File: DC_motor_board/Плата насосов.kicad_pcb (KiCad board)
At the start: 2 copper layers, 77.5 x 64.5 mm, 106 parts, among them J1 Prog, J2 OUT DG142R-5.08-02P-14, J3 OUT DG142R-5.08-02P-14, J4 IN24V DG142R-5.08-04P-14, U1 ADM3485EARZ-REEL, U2 ISO6741FDWR, U3 STM32G070RBTx, U4 AM1SS-2403SJZ, U5 BTS7960b, U6 BTS7960b, U7 BTS7960b, U8 BTS7960b, U9 ULN2003D1013TR

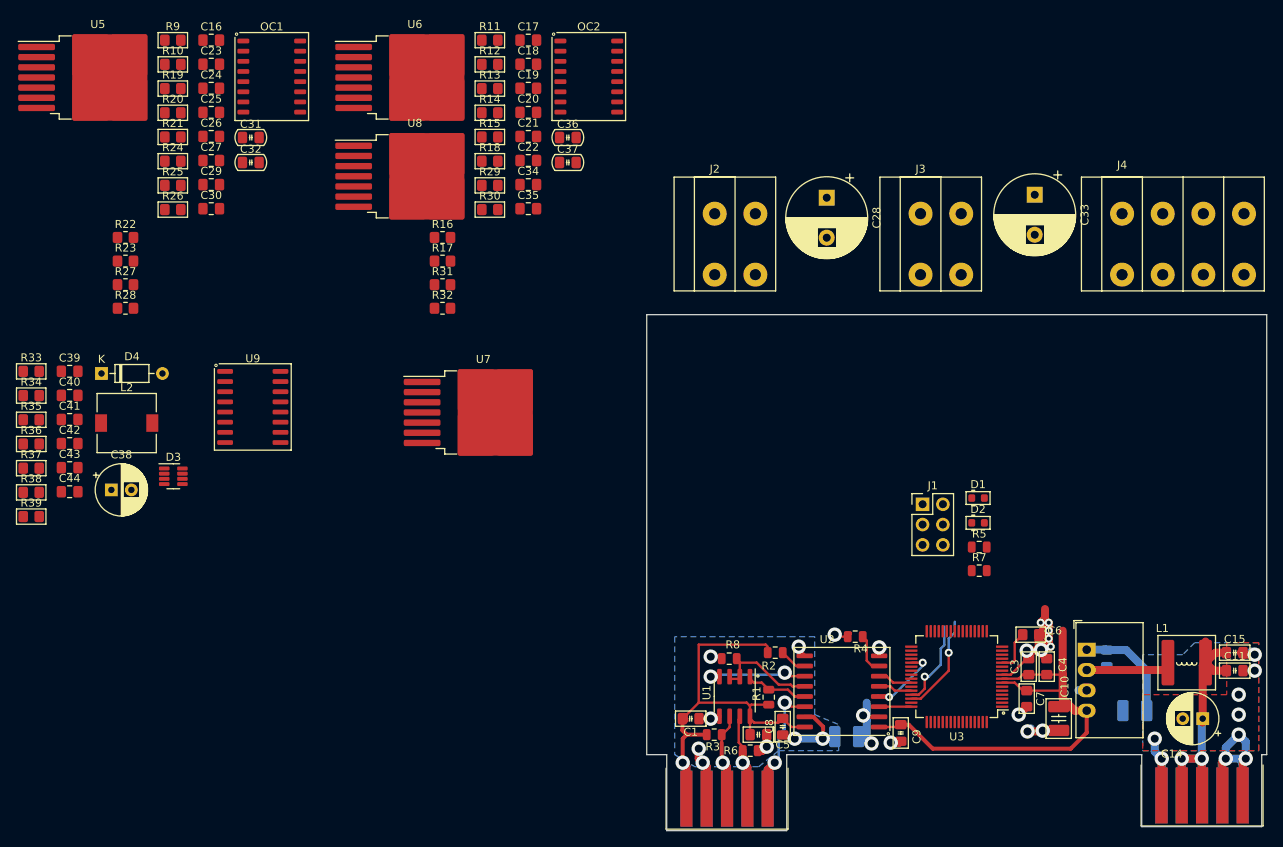
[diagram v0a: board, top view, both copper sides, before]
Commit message: Renew footprint connectors PCB
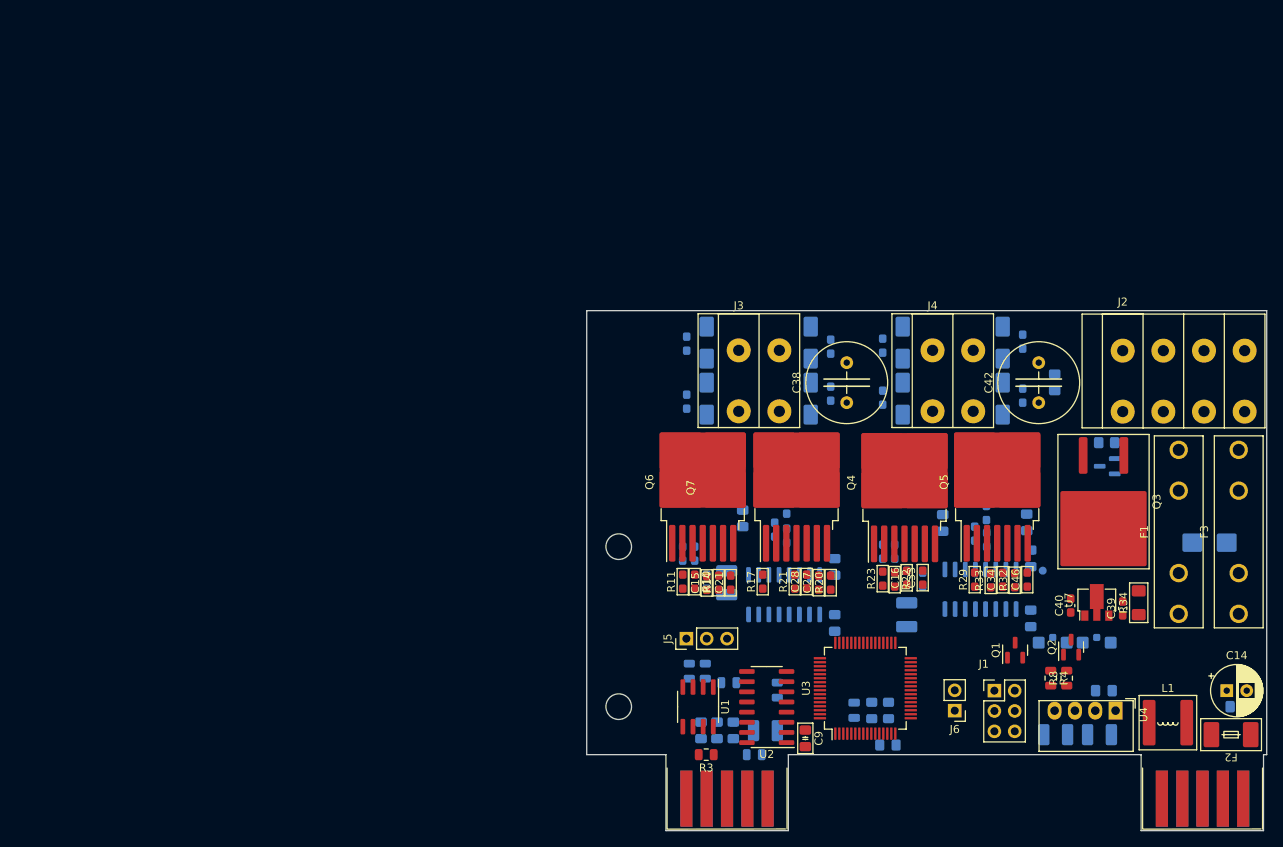
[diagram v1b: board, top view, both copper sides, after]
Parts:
- removed C43: 0,1uF 50V 0805, Capacitor_SMD:C_0805_2012Metric_Pad1.18x1.45mm_HandSolder
- removed C44: 33pF 50V 0805, Capacitor_SMD:C_0805_2012Metric_Pad1.18x1.45mm_HandSolder
- removed L2: 4,7uH 3A (MDH7045C-4R7NB=P3), Inductor_SMD:L_7.3x7.3_H4.5
- removed OC1, OC2: IS281- 4, PCM_Package_SO_AKL:SOIC-16W_5.3x10.2mm_P1.27mm
- removed R35: 104 0805, PCM_Resistor_SMD_AKL:R_0805_2012Metric_Pad1.20x1.40mm_HandSolder
- removed R36: 203 0805, PCM_Resistor_SMD_AKL:R_0805_2012Metric_Pad1.20x1.40mm_HandSolder
- removed R37: 413 0805, PCM_Resistor_SMD_AKL:R_0805_2012Metric_Pad1.20x1.40mm_HandSolder
- removed R38: 752 0805, PCM_Resistor_SMD_AKL:R_0805_2012Metric_Pad1.20x1.40mm_HandSolder
- removed R39: 912 0805, PCM_Resistor_SMD_AKL:R_0805_2012Metric_Pad1.20x1.40mm_HandSolder
- removed U8: BTS7960b, Package_TO_SOT_SMD:TO-263-7_TabPin8
- removed U9: ULN2003D1013TR, PCM_Package_SO_AKL:SO-16_5.3x10.2mm_P1.27mm
- added C45: 270 pf X7R 1206 2000v 202R18W271KW4E, PCM_Capacitor_SMD_Handsoldering_AKL:C_1210_3225Metric_Pad1.42x2.65mm, B.Cu at (129.0, 103.5)
- added C46: 1nF 50V 0603, PCM_Resistor_SMD_AKL:R_0603_1608Metric_Pad1.05x0.95mm_HandSolder, F.Cu at (144.1, 99.1)
- added D10: STPS2H100A, Diode_SMD:D_SMA, B.Cu at (141.0, 76.5)
- added D11: STPS2H100A, Diode_SMD:D_SMA, B.Cu at (117.0, 69.5)
- added D12: STPS2H100A, Diode_SMD:D_SMA, B.Cu at (141.0, 69.5)
- added D5: STPS2H100A, Diode_SMD:D_SMA, B.Cu at (104.0, 69.5)
- added D6: STPS2H100A, Diode_SMD:D_SMA, B.Cu at (128.5, 69.5)
- added D7: STPS2H100A, Diode_SMD:D_SMA, B.Cu at (104.0, 76.5)
- added D8: STPS2H100A, Diode_SMD:D_SMA, B.Cu at (128.5, 76.5)
- added D9: STPS2H100A, Diode_SMD:D_SMA, B.Cu at (117.0, 76.5)
- added F1: Fuse 5A ZH266 (2 клипсы), Fuse:Fuseholder_100_series_5x20mm_D1,5, F.Cu at (163.0, 103.4)
- added F2: 0452.500MRL, PCM_Fuse_Handsoldering_AKL:Fuse_Littelfuse-NANO2-451_453, F.Cu at (169.5, 118.5)
- added F3: Fuse 5A ZH266 (2 клипсы), Fuse:Fuseholder_100_series_5x20mm_D1,5, F.Cu at (170.5, 103.4)
- added H1: MountingHole, MountingHole:MountingHole_3.2mm_M3, F.Cu at (93.0, 95.0)
- added H2: MountingHole, MountingHole:MountingHole_3.2mm_M3, F.Cu at (93.0, 115.0)
- added J5: DebugUSART (PinHeader_01x03_P2.54mm), Connector_PinHeader_2.54mm:PinHeader_1x03_P2.54mm_Vertical, F.Cu at (101.5, 106.5)
- added J6: Debug GPIO (PinHeader_01x02_P2.54mm), Connector_PinHeader_2.54mm:PinHeader_1x02_P2.54mm_Vertical, F.Cu at (135.0, 115.5)
- added Q1: DTC114ECA (SOT-23), Package_TO_SOT_SMD:SOT-23, F.Cu at (142.6, 107.9)
- added Q2: DTC114ECA (SOT-23), Package_TO_SOT_SMD:SOT-23, F.Cu at (149.6, 107.6)
- added Q3: IRF4905SPbF (D2PAK), PCM_Package_TO_SOT_SMD_AKL:TO-263-2, F.Cu at (153.6, 89.4)
- added Q4: BTN8962TA, Package_TO_SOT_SMD:TO-263-7_TabPin8, F.Cu at (128.7, 87.0)
- added Q5: BTN8962TA, Package_TO_SOT_SMD:TO-263-7_TabPin8, F.Cu at (140.3, 86.9)
- added Q6: BTN8962TA, Package_TO_SOT_SMD:TO-263-7_TabPin8, F.Cu at (103.5, 86.9)
- added Q7: BTN8962TA, Package_TO_SOT_SMD:TO-263-7_TabPin8, F.Cu at (115.2, 86.9)
- added TP1: TestPoint, PCM_4ms_TestPoint:TestPoint_D1, B.Cu at (146.0, 98.0)
- C1, C10, C11, C5, C8, R6: moved to B.Cu
- C13, C2: value 270 pf X7R 1206 2000v 202R18W271KW4E -> 270 pf X7R 1206 2000v 202R18W271KW4E
- C15: value 0,1uF 100V 0805 -> 0,1uF 50V 0603; footprint PCM_Capacitor_SMD_AKL:C_0805_2012Metric_Pad1.18x1.45mm_HandSolder -> PCM_Capacitor_SMD_AKL:C_0603_1608Metric_Pad1.08x0.95mm_HandSolder
- C16, C34: value 0.1uF -> 0,1uF 50V 0603; footprint Capacitor_SMD:C_0805_2012Metric_Pad1.18x1.45mm_HandSolder -> PCM_Capacitor_SMD_AKL:C_0603_1608Metric_Pad1.08x0.95mm_HandSolder
- C17, C20, C24, C25, C29: value 0.1uF -> 0,22uF 100V 0603; footprint Capacitor_SMD:C_0805_2012Metric_Pad1.18x1.45mm_HandSolder -> PCM_Resistor_SMD_AKL:R_0603_1608Metric_Pad1.05x0.95mm_HandSolder; moved to B.Cu
- C18, C19, C22, C23, C30, C35: value 0.1uF -> 0,1uF 100V 0805; footprint Capacitor_SMD:C_0805_2012Metric_Pad1.18x1.45mm_HandSolder -> PCM_Capacitor_SMD_AKL:C_0805_2012Metric_Pad1.18x1.45mm_HandSolder; moved to B.Cu
- C21, C27: value 0.1uF -> 1nF 50V 0603; footprint Capacitor_SMD:C_0805_2012Metric_Pad1.18x1.45mm_HandSolder -> PCM_Resistor_SMD_AKL:R_0603_1608Metric_Pad1.05x0.95mm_HandSolder
- C26: value 0.1uF -> 270 pf X7R 1206 2000v 202R18W271KW4E; footprint Capacitor_SMD:C_0805_2012Metric_Pad1.18x1.45mm_HandSolder -> PCM_Capacitor_SMD_Handsoldering_AKL:C_1210_3225Metric_Pad1.42x2.65mm; moved to B.Cu
- C28: value 330uF 63V -> 0,1uF 50V 0603; footprint Capacitor_THT:CP_Radial_D10.0mm_P5.00mm -> PCM_Capacitor_SMD_AKL:C_0603_1608Metric_Pad1.08x0.95mm_HandSolder
- C3: value 0,1uF 50V 0805 -> 0,1uF 100V 0805; footprint PCM_Resistor_SMD_AKL:R_0805_2012Metric_Pad1.20x1.40mm_HandSolder -> PCM_Capacitor_SMD_Handsoldering_AKL:C_0805_2012Metric_Pad1.15x1.40mm; moved to B.Cu
- C31: value 470nF 50V 0805 -> 0,1uF 100V 0805; footprint PCM_Capacitor_SMD_Handsoldering_AKL:C_0805_2012Metric_Pad1.18x1.45mm -> PCM_Capacitor_SMD_AKL:C_0805_2012Metric_Pad1.18x1.45mm_HandSolder; moved to B.Cu
- C32, C36, C37: value 470nF 50V 0805 -> 0,22uF 100V 0603; footprint PCM_Capacitor_SMD_Handsoldering_AKL:C_0805_2012Metric_Pad1.18x1.45mm -> PCM_Resistor_SMD_AKL:R_0603_1608Metric_Pad1.05x0.95mm_HandSolder; moved to B.Cu
- C33: value 330uF 63V -> 1nF 50V 0603; footprint Capacitor_THT:CP_Radial_D10.0mm_P5.00mm -> PCM_Resistor_SMD_AKL:R_0603_1608Metric_Pad1.05x0.95mm_HandSolder
- C38: value 22uF 63V (К50-35) -> 330uF 50V D10 H17; footprint Capacitor_THT:CP_Radial_D6.3mm_P2.50mm -> PCM_Capacitor_THT_AKL:C_Radial_D10.0mm_H16.0mm_P5.00mm
- C39: value 0,1uF 50V 0805 -> 0,33uF 50V 0603; footprint Capacitor_SMD:C_0805_2012Metric_Pad1.18x1.45mm_HandSolder -> Capacitor_SMD:C_0603_1608Metric_Pad1.08x0.95mm_HandSolder
- C4: footprint PCM_Resistor_SMD_AKL:R_0805_2012Metric_Pad1.20x1.40mm_HandSolder -> PCM_Capacitor_SMD_AKL:C_0805_2012Metric_Pad1.15x1.40mm; moved to B.Cu
- C40: value 22uF 16V 0805 -> 0,1uF 50V 0603; footprint Capacitor_SMD:C_0805_2012Metric_Pad1.18x1.45mm_HandSolder -> Capacitor_SMD:C_0603_1608Metric_Pad1.08x0.95mm_HandSolder
- C41: value 22uF 16V 0805 -> 0,1uF 100V 0805; footprint Capacitor_SMD:C_0805_2012Metric_Pad1.18x1.45mm_HandSolder -> PCM_Capacitor_SMD_AKL:C_0805_2012Metric_Pad1.18x1.45mm_HandSolder; moved to B.Cu
- C42: value 0,1uF 50V 0805 -> 330uF 50V D10 H17; footprint Capacitor_SMD:C_0805_2012Metric_Pad1.18x1.45mm_HandSolder -> PCM_Capacitor_THT_AKL:C_Radial_D10.0mm_H16.0mm_P5.00mm
- C6: value 0,1uF 50V 0805 -> 0,1uF 100V 0805; footprint PCM_Resistor_SMD_AKL:R_0805_2012Metric_Pad1.20x1.40mm_HandSolder -> PCM_Capacitor_SMD_AKL:C_0805_2012Metric_Pad1.15x1.40mm; moved to B.Cu
- C7: value 0,1uF 50V 0805 -> 0,1uF 100V 0805; footprint PCM_Resistor_SMD_AKL:R_0805_2012Metric_Pad1.20x1.40mm_HandSolder -> PCM_Capacitor_SMD_AKL:C_0805_2012Metric; moved to B.Cu
- D1, D2: value LED 0603 -> KPA-3010CGCK; footprint PCM_Diode_SMD_AKL:D_0603_1608Metric_TVS -> LED_SMD:LED_Kingbright_KPA-3010_3x2x1mm; moved to B.Cu
- D3: value MP2315S TSOT-23-8 -> SM6T30СA (SMB); footprint Package_TO_SOT_SMD:TSOT-23-8 -> Diode_SMD:D_SMB; moved to B.Cu
- D4: value 1N4148 SOD27 -> BZX84C10 (SOT-23); footprint Diode_THT:D_DO-35_SOD27_P7.62mm_Horizontal -> Package_TO_SOT_SMD:SOT-23; moved to B.Cu
- J2: value OUT DG142R-5.08-02P-14 -> DG142R-5.08-04P-14 IN24V; footprint Connector:DG142R-5.08-02P-14 -> Connector:DG142R-5.08-04P-14
- J3: value OUT DG142R-5.08-02P-14 -> DG142R-5.08-02P-14 OUT
- J4: value IN24V DG142R-5.08-04P-14 -> DG142R-5.08-02P-14 OUT; footprint Connector:DG142R-5.08-04P-14 -> Connector:DG142R-5.08-02P-14
- R1: value 103 0805 -> 472 0805; moved to B.Cu
- R10, R11: value 511 0805 -> 104 0603; footprint PCM_Resistor_SMD_AKL:R_0805_2012Metric_Pad1.20x1.40mm_HandSolder -> PCM_Resistor_SMD_AKL:R_0603_1608Metric_Pad1.05x0.95mm_HandSolder
- R12, R13, R19: value 511 0805 -> 103 0603; footprint PCM_Resistor_SMD_AKL:R_0805_2012Metric_Pad1.20x1.40mm_HandSolder -> PCM_Resistor_SMD_AKL:R_0603_1608Metric_Pad1.05x0.95mm_HandSolder; moved to B.Cu
- R14, R20: value 511 0805 -> 102 0603; footprint PCM_Resistor_SMD_AKL:R_0805_2012Metric_Pad1.20x1.40mm_HandSolder -> PCM_Resistor_SMD_AKL:R_0603_1608Metric_Pad1.05x0.95mm_HandSolder
- R15, R26: value 103 0805 -> 102 0603; footprint PCM_Resistor_SMD_AKL:R_0805_2012Metric_Pad1.20x1.40mm_HandSolder -> PCM_Resistor_SMD_AKL:R_0603_1608Metric_Pad1.05x0.95mm_HandSolder; moved to B.Cu
- R16, R28: value 1k -> 104 0603; footprint Resistor_SMD:R_0805_2012Metric_Pad1.20x1.40mm_HandSolder -> PCM_Resistor_SMD_AKL:R_0603_1608Metric_Pad1.05x0.95mm_HandSolder; moved to B.Cu
- R17, R22, R23: value 1k -> 104 0603; footprint Resistor_SMD:R_0805_2012Metric_Pad1.20x1.40mm_HandSolder -> PCM_Resistor_SMD_AKL:R_0603_1608Metric_Pad1.05x0.95mm_HandSolder
- R18, R24, R25, R30: value 103 0805 -> 103 0603; footprint PCM_Resistor_SMD_AKL:R_0805_2012Metric_Pad1.20x1.40mm_HandSolder -> PCM_Resistor_SMD_AKL:R_0603_1608Metric_Pad1.05x0.95mm_HandSolder; moved to B.Cu
- R2: value 472 0805 -> 103 0805; moved to B.Cu
- R21: value 103 0805 -> 102 0603; footprint PCM_Resistor_SMD_AKL:R_0805_2012Metric_Pad1.20x1.40mm_HandSolder -> PCM_Resistor_SMD_AKL:R_0603_1608Metric_Pad1.05x0.95mm_HandSolder
- R27: value 1k -> 102 0603; footprint Resistor_SMD:R_0805_2012Metric_Pad1.20x1.40mm_HandSolder -> PCM_Resistor_SMD_AKL:R_0603_1608Metric_Pad1.05x0.95mm_HandSolder; moved to B.Cu
- R29: value 103 0805 -> 104 0603; footprint PCM_Resistor_SMD_AKL:R_0805_2012Metric_Pad1.20x1.40mm_HandSolder -> PCM_Resistor_SMD_AKL:R_0603_1608Metric_Pad1.05x0.95mm_HandSolder
- R31: value 1k -> 103 0603; footprint Resistor_SMD:R_0805_2012Metric_Pad1.20x1.40mm_HandSolder -> PCM_Resistor_SMD_AKL:R_0603_1608Metric_Pad1.05x0.95mm_HandSolder; moved to B.Cu
- R32: value 1k -> 102 0603; footprint Resistor_SMD:R_0805_2012Metric_Pad1.20x1.40mm_HandSolder -> PCM_Resistor_SMD_AKL:R_0603_1608Metric_Pad1.05x0.95mm_HandSolder
- R33: value 100 0805 -> 102 0603; footprint PCM_Resistor_SMD_AKL:R_0805_2012Metric_Pad1.20x1.40mm_HandSolder -> PCM_Resistor_SMD_AKL:R_0603_1608Metric_Pad1.05x0.95mm_HandSolder
- R34: value 304 0805 -> 621 1206; footprint PCM_Resistor_SMD_AKL:R_0805_2012Metric_Pad1.20x1.40mm_HandSolder -> PCM_Resistor_SMD_AKL:R_1206_3216Metric_Pad1.42x1.75mm_HandSolder
- R4: value 472 0805 -> 151 0805
- R5: value 151 0805 -> 472 0805; moved to B.Cu
- R7: value 151 0805 -> 103 0805; moved to B.Cu
- R8: value 103 0805 -> 151 0805
- R9: value 511 0805 -> 103 0805; moved to B.Cu
- U1: value ADM3485EARZ-REEL -> ADM3485EARZ-REEL (SOIC-8)
- U2: value ISO6741FDWR -> π141M30; footprint PCM_Package_SO_AKL:SOIC-16W_7.5x10.3mm_P1.27mm -> Package_SO:SOIC-16_3.9x9.9mm_P1.27mm
- U3: value STM32G070RBTx -> STM32G070RBTx (LQFP-64)
- U4: footprint Converter_DCDC:Converter_DCDC_Murata_MEE3SxxxxSC_THT -> Converter_DCDC:Converter_DCDC_Murata_MEE1SxxxxSC_THT
- U5, U6: value BTS7960b -> π162M30; footprint Package_TO_SOT_SMD:TO-263-7_TabPin8 -> Package_SO:SOIC-16_3.9x9.9mm_P1.27mm; moved to B.Cu
- U7: value BTS7960b -> L78L05 (SOT89-3); footprint Package_TO_SOT_SMD:TO-263-7_TabPin8 -> Package_TO_SOT_SMD:SOT-89-3
- moved R34 140.8 mm to (158.0, 102.0), turned to 90 degrees
- moved C39 134.9 mm to (156.0, 102.7), turned to 90 degrees
- moved D3 129.8 mm to (166.8, 94.5)
- moved C40 127.9 mm to (149.5, 102.4), turned to 90 degrees
- moved R9 127.1 mm to (154.0, 82.0), turned to 180 degrees
- moved D4 126.3 mm to (154.1, 85.0), turned to 180 degrees
- moved C41 123.2 mm to (147.5, 74.5), turned to 90 degrees
- moved R33 122.8 mm to (139.5, 99.2), turned to 90 degrees
- moved C42 121.2 mm to (145.5, 77.0), turned to 90 degrees
- moved C30 114.5 mm to (144.5, 104.0), turned to 90 degrees
- moved C31 110.8 mm to (144.5, 96.5), turned to 90 degrees
- moved R28 110.6 mm to (139.0, 90.8), turned to 90 degrees
- moved C16 109.9 mm to (129.0, 98.9), turned to 90 degrees
- moved C23 107.9 mm to (133.5, 92.0), turned to 90 degrees
- moved U5 107.4 mm to (113.7, 101.0), turned to 90 degrees
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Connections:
- net /DE renamed /DE_USART_1
- net /DI renamed /RX_USART_1
- net /RO renamed /TX_USART_1
- C15 pad 1: +24V -> GND2
- C15 pad 2: GNDA -> Net-(Q6-SR)
- C16 pad 1: +3V3 -> GND2
- C16 pad 2: GNDD -> Net-(Q4-SR)
- C17 pad 1: +3V3 -> Net-(D5-K)
- C17 pad 2: GNDD -> /+24VOUT
- C18 pad 1: /+5V -> GNDD
- C18 pad 2: GND2 -> +3V3
- C19 pad 1: +3V3 -> +5V
- C19 pad 2: GNDD -> GND2
- C20 pad 1: /+5V -> GND2
- C20 pad 2: GND2 -> Net-(D5-K)
- C21 pad 1: +3V3 -> GND2
- C21 pad 2: GNDD -> Net-(Q6-IS)
- C22 pad 1: /+5V -> /+24VOUT
- C23 pad 1: /+5V -> /+24VOUT
- C24 pad 1: +3V3 -> Net-(D11-K)
- C24 pad 2: GNDD -> /+24VOUT
- C25 pad 1: /+5V -> GND2
- C25 pad 2: GND2 -> Net-(D11-K)
- C26 pad 1: +3V3 -> GNDD
- C26 pad 2: GNDD -> GND2
- C27 pad 1: /+5V -> GND2
- C27 pad 2: GND2 -> Net-(Q7-IS)
- C28 pad 1: /+24VOUT -> GND2
- C28 pad 2: GNDA -> Net-(Q7-SR)
- C29 pad 1: +3V3 -> Net-(D6-K)
- C29 pad 2: GNDD -> /+24VOUT
- C30 pad 1: /+5V -> GNDD
- C30 pad 2: GND2 -> +3V3
- C31 pad 1: GNDA -> +5V
- C31 pad 2: /+24VOUT -> GND2
- C32 pad 1: GNDA -> GND2
- C32 pad 2: /+24VOUT -> Net-(D6-K)
- C33 pad 1: /+24VOUT -> GND2
- C33 pad 2: GNDA -> Net-(Q4-IS)
- C34 pad 1: +3V3 -> GND2
- C34 pad 2: GNDD -> Net-(Q5-SR)
- C35 pad 1: /+5V -> /+24VOUT
- C36 pad 1: GNDA -> Net-(D10-A)
- C37 pad 1: GNDA -> GND2
- C37 pad 2: /+24VOUT -> Net-(D10-A)
- C38 pad 2: GNDD -> GND2
- C39 pad 1: GNDD -> Net-(U7-IN)
- C39 pad 2: /+24VOUT -> GND2
- C40 pad 1: GNDD -> +5V
- C40 pad 2: /+5V -> GND2
- C41 pad 1: GNDD -> /+24VOUT
- C41 pad 2: /+5V -> GND2
- C42 pad 1: Net-(D4-K) -> /+24VOUT
- C42 pad 2: Net-(D3-SW) -> GND2
- D3 pad 2: /+24VOUT -> GND2
- D4 pad 1: Net-(D4-K) -> Net-(D4-A)
- D4 pad 2: Net-(D3-VCC) -> unconnected-(D4-NC-Pad2)
- J2 pad 2: Net-(J2-Pin_2) -> Net-(J2-Pin_1)
- J3 pad 1: Net-(J3-Pin_1) -> Net-(D5-K)
- J3 pad 2: Net-(J3-Pin_2) -> Net-(D11-K)
- J4 pad 1: /+24VOUT -> Net-(D6-K)
- J4 pad 2: /+24VOUT -> Net-(D10-A)
- R1 pad 1: Net-(U1-RO) -> Net-(U2-VE2)
- R10 pad 1: +3V3 -> Net-(Q6-INH)
- R10 pad 2: Net-(OC1-Pad5) -> GND2
- R11 pad 1: +3V3 -> GND2
- R11 pad 2: Net-(OC2-Pad7) -> Net-(Q6-IN)
- R12 pad 1: +3V3 -> Net-(U5-VOD)
- R12 pad 2: Net-(OC2-Pad5) -> Net-(Q6-INH)
- R13 pad 1: +3V3 -> Net-(Q6-IN)
- R13 pad 2: Net-(OC2-Pad3) -> Net-(U5-VOC)
- R14 pad 1: +3V3 -> GND2
- R14 pad 2: Net-(OC2-Pad1) -> Net-(Q6-IS)
- R15 pad 1: Net-(OC2-Pad15) -> GND2
- R15 pad 2: Net-(U6-IN) -> Net-(Q6-SR)
- R16 pad 1: GND2 -> Net-(Q7-INH)
- R16 pad 2: Net-(U6-SR) -> GND2
- R17 pad 2: Net-(U6-IS) -> Net-(Q7-IN)
- R18 pad 1: Net-(OC2-Pad13) -> Net-(U5-VOA)
- R18 pad 2: Net-(U6-INH) -> Net-(Q7-INH)
- R19 pad 1: +3V3 -> Net-(Q7-IN)
- R19 pad 2: Net-(OC1-Pad3) -> Net-(U5-VOB)
- R2 pad 1: Net-(U2-EN2) -> Net-(U1-RO)
- R20 pad 1: +3V3 -> GND2
- R20 pad 2: Net-(OC1-Pad1) -> Net-(Q7-IS)
- R21 pad 1: Net-(OC1-Pad15) -> GND2
- R21 pad 2: Net-(U5-IN) -> Net-(Q7-SR)
- R22 pad 1: GND2 -> Net-(Q4-INH)
- R22 pad 2: Net-(U5-SR) -> GND2
- R23 pad 2: Net-(U5-IS) -> Net-(Q4-IN)
- R24 pad 1: Net-(OC1-Pad13) -> Net-(U6-VOD)
- R24 pad 2: Net-(U5-INH) -> Net-(Q4-INH)
- R25 pad 1: Net-(OC1-Pad11) -> Net-(Q4-IN)
- R25 pad 2: Net-(U7-IN) -> Net-(U6-VOC)
- R26 pad 1: Net-(OC1-Pad9) -> GND2
- R26 pad 2: Net-(U7-INH) -> Net-(Q4-IS)
- R27 pad 2: Net-(U7-SR) -> Net-(Q4-SR)
- R28 pad 1: GND2 -> Net-(Q5-INH)
- R28 pad 2: Net-(U7-IS) -> GND2
- R29 pad 1: Net-(OC2-Pad11) -> GND2
- R29 pad 2: Net-(U8-IN) -> Net-(Q5-IN)
- R30 pad 1: Net-(OC2-Pad9) -> Net-(U6-VOA)
- R30 pad 2: Net-(U8-INH) -> Net-(Q5-INH)
- R31 pad 1: GND2 -> Net-(Q5-IN)
- R31 pad 2: Net-(U8-SR) -> Net-(U6-VOB)
- R32 pad 2: Net-(U8-IS) -> Net-(Q5-IS)
- R33 pad 1: Net-(D3-BST) -> GND2
- R33 pad 2: Net-(D4-K) -> Net-(Q5-SR)
- R34 pad 1: /+24VOUT -> Net-(U7-IN)
- R34 pad 2: Net-(D3-EN) -> /+24VOUT
- R4 pad 1: +3V3 -> Net-(D1-A)
- R4 pad 2: Net-(U2-EN1) -> +3V3
- R5 pad 1: Net-(D1-K) -> +3V3
- R5 pad 2: GNDD -> Net-(U2-VE1)
- R7 pad 1: Net-(D2-K) -> GND1
- R7 pad 2: GNDD -> Net-(U1-DE)
- R8 pad 1: GND1 -> +3V3
- R8 pad 2: Net-(U1-DE) -> Net-(D2-A)
- R9 pad 1: +3V3 -> Net-(D4-A)
- R9 pad 2: Net-(OC1-Pad7) -> GND2
- RS2 pad 2: +24V -> Net-(RS2-Pin_2)
- RS2 pad 3: +24V -> Net-(RS2-Pin_2)
- RS2 pad 8: +24V -> Net-(RS2-Pin_2)
- RS2 pad 9: +24V -> Net-(RS2-Pin_2)
- U2 pad 10: Net-(U2-EN2) -> Net-(U2-VE2)
- U2 pad 11: Net-(U1-DI) -> Net-(U1-RO)
- U2 pad 13: Net-(U1-RO) -> Net-(U1-DI)
- U2 pad 7: Net-(U2-EN1) -> Net-(U2-VE1)
- U3 pad 17: /LED_ON_1 -> unconnected-(U3-PA0-Pad17)
- U3 pad 18: /FT_ON_1 -> unconnected-(U3-PA1-Pad18)
- U3 pad 19: /LED_ON_2 -> unconnected-(U3-PA2-Pad19)
- U3 pad 20: /FT_ON_2 -> unconnected-(U3-PA3-Pad20)
- U3 pad 21: Net-(D1-A) -> Net-(Q1-B)
- U3 pad 22: Net-(D2-A) -> Net-(Q2-B)
- U3 pad 25: unconnected-(U3-PC4-Pad25) -> /GPIO1
- U3 pad 26: unconnected-(U3-PC5-Pad26) -> /GPIO2
- U3 pad 27: unconnected-(U3-PB0-Pad27) -> /IS2_2
- U3 pad 28: unconnected-(U3-PB1-Pad28) -> /IS1_1
- U3 pad 29: unconnected-(U3-PB2-Pad29) -> /IS2_1
- U3 pad 36: unconnected-(U3-PA8-Pad36) -> /IS1_2
- U3 pad 39: unconnected-(U3-PC7-Pad39) -> /UART_DE
- U3 pad 40: unconnected-(U3-PD8-Pad40) -> /UART_TX
- U3 pad 41: unconnected-(U3-PD9-Pad41) -> /UART_RX
- U5 pad 1: GND2 -> +3V3
- U5 pad 2: Net-(U5-IN) -> /Enable_2
- U5 pad 3: Net-(U5-INH) -> /Forward_2
- U5 pad 4: Net-(J2-Pin_1) -> /Back_2
- U5 pad 5: Net-(U5-SR) -> /Enable_2
- U5 pad 6: Net-(U5-IS) -> /IS2_2
- U5 pad 7: /+24VOUT -> /IS1_2
- U5 pad 8: Net-(J2-Pin_1) -> GNDD
- U6 pad 1: GND2 -> +3V3
- U6 pad 2: Net-(U6-IN) -> /Enable_1
- U6 pad 3: Net-(U6-INH) -> /Forward_1
- U6 pad 4: Net-(J3-Pin_1) -> /Back_1
- U6 pad 5: Net-(U6-SR) -> /Enable_1
- U6 pad 6: Net-(U6-IS) -> /IS2_1
- U6 pad 7: /+24VOUT -> /IS1_1
- U6 pad 8: Net-(J3-Pin_1) -> GNDD
- U7 pad 1: GND2 -> +5V
- U7 pad 2: Net-(U7-IN) -> GNDA
- U7 pad 3: Net-(U7-INH) -> Net-(U7-IN)
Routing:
- net +3V3: track 61.6 -> 0.00 mm, vias 1 -> 0
- net /+3.3VRS485: track 58.9 -> 0.00 mm, vias 1 -> 0
- net GNDA: track 57.0 -> 0.00 mm, vias 9 -> 0
- net +24V: track 44.5 -> 0.00 mm, vias 2 -> 0
- net GNDD: track 39.1 -> 0.00 mm, vias 14 -> 0
- net GND1: track 25.0 -> 0.00 mm, vias 8 -> 0
- net /RTS: track 21.8 -> 0.00 mm, vias 2 -> 0
- net Net-(RS1-Pin_4): track 15.5 -> 0.00 mm, vias 1 -> 0
- net Net-(RS1-Pin_3): track 15.4 -> 0.00 mm, vias 1 -> 0
- net Net-(U1-DE): track 14.1 -> 0.00 mm
- net Net-(U1-DI): track 13.4 -> 0.00 mm, vias 2 -> 0
- net Net-(U4-IN+): track 13.0 -> 0.00 mm
- net /SWCLK: track 12.5 -> 0.00 mm, vias 1 -> 0
- net /SWDIO: track 11.1 -> 0.00 mm, vias 1 -> 0
- net /TX_USART_1: track 9.11 -> 0.00 mm, vias 2 -> 0
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- removed copper zone on B.Cu, net GND1
- removed copper zone on B.Cu, net GNDA
- removed copper zone on F.Cu, net GNDA
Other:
- board size 77.5 x 64.5 mm -> 85 x 65 mm

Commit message: Renew pin Prog connectors and schem Analog IO
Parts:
- J1: value Prog -> Prog (PinHeader_2x03_P2.54mm)
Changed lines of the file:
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@@
     (property "Sheetfile" "Плата насосов.kicad_sch")
     (property "Sheetname" "")
-    (property "ki_description" "Generic connector, double row, 02x03, counter clockwise pin numbering scheme (similar to DIP package numbering), script generated (kicad-library-utils/schlib/autogen/connector/)")
+    (property "ki_description" "Generic connector, double row, 02x03, odd/even pin numbering scheme (row 1 odd numbers, row 2 even numbers), script generated (kicad-library-utils/schlib/autogen/connector/)")
     (property "ki_keywords" "connector")
     (attr through_hole)
@@
         (effects (font (size 1 1) (thickness 0.15)))
     )
-    (fp_text value "Prog" (at -1.33 6.41) (layer "F.Fab")
+    (fp_text value "Prog (PinHeader_2x03_P2.54mm)" (at -1.33 6.41) (layer "F.Fab")
         (effects (font (size 1 1) (thickness 0.15)))
     )
@@
       (net 13 "/SWCLK") (pinfunction "Pin_3") (pintype "passive"))
     (pad "4" thru_hole oval (at 2.54 2.54) (size 1.7 1.7) (drill 1) (layers "*.Cu" "*.Mask")
-      (net 34 "unconnected-(J1-Pin_4-Pad4)") (pinfunction "Pin_4") (pintype "passive"))
+      (net 34 "unconnected-(J1-Pin_4-Pad4)") (pinfunction "Pin_4") (pintype "passive+no_connect"))
     (pad "5" thru_hole oval (at 0 5.08) (size 1.7 1.7) (drill 1) (layers "*.Cu" "*.Mask")
       (net 6 "/NRST") (pinfunction "Pin_5") (pintype "passive"))

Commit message: renew all schems and pcb for production
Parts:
- added TP10: TestPoint, PCM_4ms_TestPoint:TestPoint_D1, F.Cu at (87.2, 82.7)
- added TP11: TestPoint, PCM_4ms_TestPoint:TestPoint_D1, F.Cu at (71.2, 78.7)
- added TP12: TestPoint, PCM_4ms_TestPoint:TestPoint_D1, F.Cu at (71.2, 70.7)
- added TP13: TestPoint, PCM_4ms_TestPoint:TestPoint_D1, F.Cu at (71.2, 80.7)
- added TP14: TestPoint, PCM_4ms_TestPoint:TestPoint_D1, F.Cu at (71.2, 72.7)
- added TP15: TestPoint, PCM_4ms_TestPoint:TestPoint_D1, F.Cu at (71.2, 82.7)
- added TP16: TestPoint, PCM_4ms_TestPoint:TestPoint_D1, F.Cu at (71.2, 74.7)
- added TP17: TestPoint, PCM_4ms_TestPoint:TestPoint_D1, F.Cu at (73.2, 78.7)
- added TP18: TestPoint, PCM_4ms_TestPoint:TestPoint_D1, F.Cu at (73.2, 70.7)
- added TP19: TestPoint, PCM_4ms_TestPoint:TestPoint_D1, F.Cu at (73.2, 80.7)
- added TP2: TestPoint, PCM_4ms_TestPoint:TestPoint_D1, F.Cu at (83.2, 78.7)
- added TP20: TestPoint, PCM_4ms_TestPoint:TestPoint_D1, F.Cu at (73.2, 72.7)
- added TP21: TestPoint, PCM_4ms_TestPoint:TestPoint_D1, F.Cu at (73.2, 82.7)
- added TP22: TestPoint, PCM_4ms_TestPoint:TestPoint_D1, F.Cu at (73.2, 74.7)
- added TP23: TestPoint, PCM_4ms_TestPoint:TestPoint_D1, F.Cu at (75.2, 78.7)
- added TP24: TestPoint, PCM_4ms_TestPoint:TestPoint_D1, F.Cu at (75.2, 70.7)
- added TP25: TestPoint, PCM_4ms_TestPoint:TestPoint_D1, F.Cu at (75.2, 80.7)
- added TP26: TestPoint, PCM_4ms_TestPoint:TestPoint_D1, F.Cu at (75.2, 72.7)
- added TP27: TestPoint, PCM_4ms_TestPoint:TestPoint_D1, F.Cu at (75.2, 82.7)
- added TP28: TestPoint, PCM_4ms_TestPoint:TestPoint_D1, F.Cu at (75.2, 74.7)
- added TP29: TestPoint, PCM_4ms_TestPoint:TestPoint_D1, F.Cu at (77.2, 78.7)
- added TP3: TestPoint, PCM_4ms_TestPoint:TestPoint_D1, F.Cu at (83.2, 80.7)
- added TP30: TestPoint, PCM_4ms_TestPoint:TestPoint_D1, F.Cu at (77.2, 70.7)
- added TP31: TestPoint, PCM_4ms_TestPoint:TestPoint_D1, F.Cu at (77.2, 80.7)
- added TP32: TestPoint, PCM_4ms_TestPoint:TestPoint_D1, F.Cu at (77.2, 72.7)
- added TP33: TestPoint, PCM_4ms_TestPoint:TestPoint_D1, F.Cu at (77.2, 82.7)
- added TP34: TestPoint, PCM_4ms_TestPoint:TestPoint_D1, F.Cu at (77.2, 74.7)
- added TP35: TestPoint, PCM_4ms_TestPoint:TestPoint_D1, F.Cu at (79.2, 78.7)
- added TP36: TestPoint, PCM_4ms_TestPoint:TestPoint_D1, F.Cu at (79.2, 70.7)
- added TP37: TestPoint, PCM_4ms_TestPoint:TestPoint_D1, F.Cu at (79.2, 80.7)
- added TP38: TestPoint, PCM_4ms_TestPoint:TestPoint_D1, F.Cu at (79.2, 72.7)
- added TP39: TestPoint, PCM_4ms_TestPoint:TestPoint_D1, F.Cu at (79.2, 82.7)
- added TP4: TestPoint, PCM_4ms_TestPoint:TestPoint_D1, F.Cu at (83.2, 82.7)
- added TP40: TestPoint, PCM_4ms_TestPoint:TestPoint_D1, F.Cu at (79.2, 74.7)
- added TP5: TestPoint, PCM_4ms_TestPoint:TestPoint_D1, F.Cu at (85.2, 78.7)
- added TP6: TestPoint, PCM_4ms_TestPoint:TestPoint_D1, F.Cu at (85.2, 80.7)
- added TP7: TestPoint, PCM_4ms_TestPoint:TestPoint_D1, F.Cu at (85.2, 82.7)
- added TP8: TestPoint, PCM_4ms_TestPoint:TestPoint_D1, F.Cu at (87.2, 78.7)
- added TP9: TestPoint, PCM_4ms_TestPoint:TestPoint_D1, F.Cu at (87.2, 80.7)
- C8: moved to F.Cu
- R1, R5: value 472 0805 -> 0805-4,7 кОм±5%-0,125 Вт; moved to F.Cu
- R10, R11, R16, R17, R22, R23, R28, R29: value 104 0603 -> 0603-100 кОм±5%-0,062 Вт
- R12, R13, R18, R19, R24, R25, R30, R31: value 103 0603 -> 0603-10 кОм±5%-0,062 Вт
- R14, R15, R20, R21, R26, R27, R32, R33: value 102 0603 -> 0603-1 кОм±5%-0,062 Вт
- R2: value 103 0805 -> 0805-10 кОм±5%-0,125 Вт; moved to F.Cu
- R3, R6: value 561 0805 -> 0805-560 Ом±5%-0,125 Вт
- R34: value 621 1206 -> 1206-620 Ом±5%-0,25 Вт
- R4, R8: value 151 0805 -> 0805-150 Ом±5%-0,125 Вт
- R7, R9: value 103 0805 -> 0805-10 кОм±5%-0,125 Вт
- U2: value π141M30 -> pia141M30 (SOIC-16)
- U5, U6: value π162M30 -> pia162M30 (SOIC-16)
- moved D2 9.11 mm to (143.7, 107.1), turned to 180 degrees
- moved Q1 6.06 mm to (148.6, 107.6)
- moved J5 5.34 mm to (106.8, 106.6), turned to -90 degrees
- moved Q2 4.90 mm to (144.7, 107.2), turned to 180 degrees
- moved R5 4.27 mm to (113.9, 108.8), turned to 0 degrees
- moved R7 3.87 mm to (103.9, 113.8), turned to 180 degrees
- moved R8 3.60 mm to (145.4, 111.4)
- moved R34 3.58 mm to (155.8, 104.8), turned to 180 degrees
- moved D1 2.21 mm to (149.4, 107.0), turned to 180 degrees
- moved C26 2.20 mm to (106.6, 101.7)
- moved C7 2.12 mm to (122.1, 117.5), turned to -90 degrees
- moved U7 1.97 mm to (154.3, 100.5)
- moved C39 1.97 mm to (157.5, 101.5)
- moved C40 1.97 mm to (151.0, 101.1)
- moved J6 1.31 mm to (134.4, 114.3)
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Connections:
- U7 pad 2: GNDA -> GND2
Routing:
- net +3V3: track 0.00 -> 119.2 mm, vias 0 -> 4
- net GNDD: track 0.00 -> 49.9 mm, vias 0 -> 5
- net /+3.3VRS485: track 0.00 -> 44.7 mm, vias 0 -> 2
- net GND1: track 0.00 -> 34.6 mm, vias 0 -> 4
- net GNDA: track 0.00 -> 30.7 mm, vias 0 -> 16
- net /UART_RX: track 0.00 -> 28.8 mm, vias 0 -> 1
- net /UART_TX: track 0.00 -> 28.2 mm, vias 0 -> 1
- net /SWDIO: track 0.00 -> 27.3 mm, vias 0 -> 1
- net Net-(RS2-Pin_2): track 0.00 -> 26.7 mm, vias 0 -> 2
- net /SWCLK: track 0.00 -> 26.4 mm, vias 0 -> 1
- net Net-(Q1-B): track 0.00 -> 23.8 mm
- net Net-(Q2-B): track 0.00 -> 22.0 mm
- net /UART_DE: track 0.00 -> 21.1 mm, vias 0 -> 2
- net /TX_USART_1: track 0.00 -> 19.5 mm, vias 0 -> 2
- net Net-(RS1-Pin_4): track 0.00 -> 17.6 mm, vias 0 -> 1
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- added copper zone on B.Cu, net GND1
- added copper zone on F.Cu, net GND1
- added copper zone on B.Cu, net GNDA
- added copper zone on F.Cu, net GNDA
- added copper zone on B.Cu, net GNDD
- added copper zone on F.Cu, net GNDD
